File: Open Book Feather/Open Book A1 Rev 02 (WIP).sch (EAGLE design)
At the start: 124 parts, among them J1 SJ-43514-SMT, J2 10118193-0001LF, Q1 DMG341, Q2 IRLML0100, SW1 SPDT_SWITCH, U1 AP2112-3.3, U2 MCP73831T-2ACI/OT, U3 ATSAMD51J64-TQFP(10X10), U4 GD25Q16C (or GD25Q32C), U5 74AC165D, U6 GD25Q16C (or GD25Q32C), U7 23K256-I/SN, U8 MAX4466EXK+T, X1 JSTPH, X2 2x5 0.05" SWD

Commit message: renumber passives, update silkscreen
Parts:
- removed C35: 10uF, microbuilder:CAP_CERAMIC0805-NOOUTLINE
- removed R26, R27: 100K, resistor array:EXB-V8V103JV
- added C13: 1uF, microbuilder:CAP_CERAMIC0805-NOOUTLINE
- added R6: 270, microbuilder:RESISTOR0805_NOOUTLINE
- added R7: 100K, microbuilder:RESISTOR0805_NOOUTLINE
- C17: value 1uF -> 1uF/25V
- C23: value 1uF/25V -> 4.7uF/25V
- C24: value 4.7uF/25V -> 10uF; device microbuilder:CAP_CERAMIC0805-NOOUTLINE -> microbuilder:CAP_CERAMIC0805_10MGAP
- C25: value 10uF -> 1uF
- C26: value 1uF -> 10uF; device microbuilder:CAP_CERAMIC0805_10MGAP -> microbuilder:CAP_CERAMIC0805-NOOUTLINE
- C27: value 10uF -> 1uF; device microbuilder:CAP_CERAMIC0805-NOOUTLINE -> microbuilder:CAP_CERAMIC0805_10MGAP
- C29: value 1uF -> 100uF; device microbuilder:CAP_CERAMIC0805_10MGAP -> resistor:C-USC1210
- C31: value 100uF -> 0.1µF; device resistor:C-USC1210 -> microbuilder:CAP_CERAMIC0805-NOOUTLINE
- C32: value 0.1µF -> 0.01uF
- C33: value 0.01uF -> 100pF
- C34: value 100pF -> 10uF
- R10: value 1M -> 0.47ohm; device microbuilder:RESISTOR0805_NOOUTLINE -> microbuilder:RESISTOR0805_10MGAP
- R11: value 1M -> 100K; device microbuilder:RESISTOR0805_NOOUTLINE -> resistor array:EXB-V8V103JV
- R12: device microbuilder:RESISTOR0805_NOOUTLINE -> resistor array:EXB-V8V103JV
- R13: device microbuilder:RESISTOR0805_NOOUTLINE -> microbuilder:RESISTOR_0805MP
- R14: value 100K -> 1K; device microbuilder:RESISTOR0805_NOOUTLINE -> microbuilder:RESISTOR_0805MP
- R15: value 100K -> 100
- R16: value 0.47ohm -> 100; device microbuilder:RESISTOR0805_10MGAP -> microbuilder:RESISTOR0805_NOOUTLINE
- R17, R18: value 1K -> 100; device microbuilder:RESISTOR_0805MP -> microbuilder:RESISTOR0805_NOOUTLINE
- R19, R20: value 100 -> 1K
- R21, R22: value 100 -> 1M
- R24: value 1K -> 100K
- R8: value 270 -> 100K
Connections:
- net +3V3: now also C13.1, C16.2, C24.1, R11.5, R7.1; no longer C14.1, C17.2, C29.1, R26.5, R9.1
- net A0: now also R15.2; no longer R19.2
- net A1: now also R17.2; no longer R21.2
- net A10_MICAMP: now also C33.1, R24.2; no longer C34.1, R12.2
- net A6_VMEAS: now also R8.2, R9.1; no longer R14.1, R15.2
- net A7_MIC: now also C32.1, R19.1; no longer C33.1, R13.1
- net A8_: now also R13.1; no longer R17.1
- net A9_: now also R14.1; no longer R18.1
- net AGND: now also C31.2, C34.2, R16.1, R18.1, R21.1; no longer C32.2, C35.2, R10.1, R20.1, R22.1
- net AUDIO_LEFT: now also C30.2; no longer C31.2
- net AUDIO_RIGHT: now also C29.2; no longer C30.2
- net AVCC: now also R20.2, R22.2; no longer R11.2, R23.2
- net BUTTON0: now also R12.1; no longer R27.1
- net BUTTON1: now also R12.2; no longer R27.2
- net BUTTON2: now also R12.3; no longer R27.3
- net BUTTON3: now also R12.4; no longer R27.4
- net BUTTON4: now also R11.3; no longer R26.3
- net BUTTON5: now also R11.2; no longer R26.2
- net BUTTON6: now also R11.1; no longer R26.1
- net BUTTON7: now also R11.4; no longer R26.4
- net D13: now also R6.1; no longer R8.1
- net D2_A8: now also R13.2; no longer R17.2
- net D3_A9: now also R14.2; no longer R18.2
- net GND: now also C13.2, C14.1, C21.2, C24.2, R10.2, R11.6, R11.7, R11.8, R12.5, R12.6, R12.7, R12.8, R9.2; no longer C14.2, C21.1, C23.2, C29.2, R14.2, R16.2, R26.6, R26.7, R26.8, R27.5, R27.6, R27.7, R27.8
- net N$15: now also C30.1, R17.1, R18.2; no longer C31.1, R21.1, R22.2
- net N$2: now also C23.2; no longer C24.2
- net N$3: now also C23.1; no longer C24.1
- net N$65: now also C31.1, R19.2, R20.1; no longer C32.1, R13.2, R23.1
- net N$67: now also C32.2, R21.2, R22.1; no longer C33.2, R10.2, R11.1
- net N$68: now also C33.2, R23.1; no longer C34.2, R12.1
- net N$69: now also C34.1, R23.2; no longer C35.1, R24.2
- net N$7: now also R6.2; no longer R8.2
- net N$70: now also C29.1, R15.1, R16.2; no longer C30.1, R19.1, R20.2
- net PREVGH: now also C22.1; no longer C23.1
- net PREVGL: now also C21.1; no longer C22.1
- net QSPI_CS: now also R7.2; no longer R9.2
- net RESE: now also R10.1; no longer R16.1
- net VBAT: now also R8.1; no longer R15.1
- net VCOM: now also C20.2; no longer C21.2
- net VDD: now also C17.2; no longer C18.2
- net VGH: now also C15.2; no longer C16.2
- net VGL: now also C14.2; no longer C15.2
- net VSH: now also C18.2; no longer C19.2
- net VSL: now also C19.2; no longer C20.2
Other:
- note added: "Low pass F3db = 1/R23*C34*2pi"
- note added: "R23"
- note added: "R24"
- note added: "≈ 100x gain"
- note removed: "= ~25-125x gain"
- note removed: "Low pass F3db = 1/R5*C4*2pi"
- note removed: "R5"
- note removed: "VR1+R7"
- moved on the sheet: C14, C15, C16, C17, C18, C19, C20, C21, C22, C23, C24, C25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

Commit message: correct component values
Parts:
- L1: value 68uH -> 10uH
- R4, R6: value 270 -> 1K
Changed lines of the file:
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@@
 <part name="C23" library="microbuilder" deviceset="CAP_CERAMIC" device="0805-NOOUTLINE" value="4.7uF/25V"/>
 <part name="D4" library="microbuilder" deviceset="DIODE-SCHOTTKY" device="SOD-123" value="MBR0530"/>
-<part name="L1" library="microbuilder" deviceset="INDUCTOR" device="NR401" value="68uH"/>
+<part name="L1" library="microbuilder" deviceset="INDUCTOR" device="NR401" value="10uH"/>
 <part name="R10" library="microbuilder" deviceset="RESISTOR" device="0805_10MGAP" value="0.47ohm"/>
 <part name="U$10" library="microbuilder" deviceset="GND" device=""/>
@@
 <part name="R1" library="microbuilder" deviceset="RESISTOR" device="0805_NOOUTLINE" value="10K"/>
 <part name="U2" library="microbuilder" deviceset="MCP73831/2" device="" value="MCP73831T-2ACI/OT"/>
-<part name="R4" library="microbuilder" deviceset="RESISTOR" device="0805_NOOUTLINE" value="270"/>
+<part name="R4" library="microbuilder" deviceset="RESISTOR" device="0805_NOOUTLINE" value="1K"/>
 <part name="C4" library="microbuilder" deviceset="CAP_CERAMIC" device="0805-NOOUTLINE" value="10µF"/>
 <part name="U$33" library="microbuilder" deviceset="GND" device=""/>
@@
 <part name="+3V29" library="supply1" deviceset="+3V3" device=""/>
 <part name="R7" library="microbuilder" deviceset="RESISTOR" device="0805_NOOUTLINE" value="100K"/>
-<part name="R6" library="microbuilder" deviceset="RESISTOR" device="0805_NOOUTLINE" value="270"/>
+<part name="R6" library="microbuilder" deviceset="RESISTOR" device="0805_NOOUTLINE" value="1K"/>
 <part name="GND10" library="supply1" deviceset="GND" device=""/>
 <part name="FB2" library="microbuilder" deviceset="FERRITE" device="0805" value="Ferrite"/>
@@
 <instance part="R6" gate="G$1" x="185.42" y="162.56" smashed="yes" rot="R270">
 <attribute name="NAME" x="187.96" y="162.56" size="1.27" layer="95" font="vector" rot="R270" align="center"/>
-<attribute name="VALUE" x="185.42" y="162.56" size="1.016" layer="96" font="vector" ratio="15" rot="R270" align="center"/>
+<attribute name="VALUE" x="182.88" y="162.56" size="1.016" layer="96" font="vector" ratio="15" rot="R270" align="center"/>
 </instance>
 <instance part="GND10" gate="1" x="185.42" y="142.24" smashed="yes" rot="MR0">

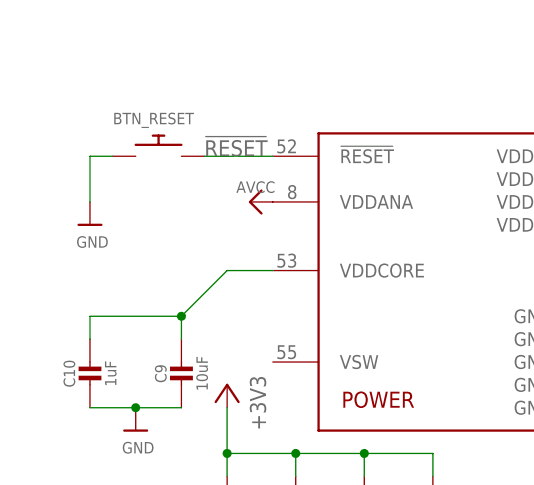
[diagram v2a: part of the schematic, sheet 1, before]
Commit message: restore reset stability circuit
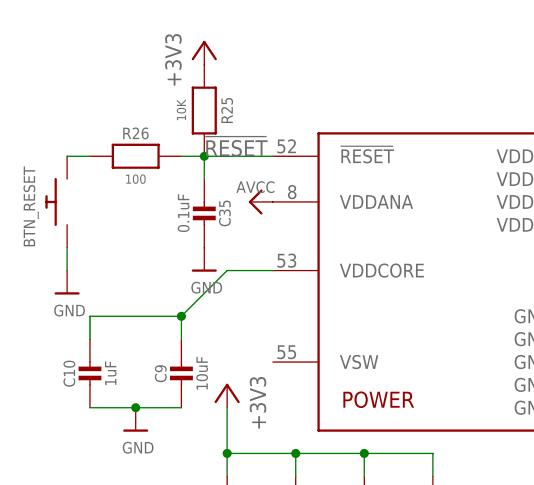
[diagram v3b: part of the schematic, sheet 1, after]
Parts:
- added C35: 0.1uF, microbuilder:CAP_CERAMIC0805_10MGAP
- added R25: 10K, microbuilder:RESISTOR0805_10MGAP
- added R26: 100, microbuilder:RESISTOR0805_10MGAP
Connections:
- new net N$1: BTN_RESET.P$2, R26.1
- net !RESET: now also C35.2, R25.2, R26.2; no longer BTN_RESET.P$2
- net +3V3: now also R25.1
- net GND: now also C35.1
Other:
- moved on the sheet: BTN_RESET
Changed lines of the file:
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@@
 <part name="+3V21" library="supply1" library_urn="urn:adsk.eagle:library:371" deviceset="+3V3" device=""/>
 <part name="GND9" library="supply1" library_urn="urn:adsk.eagle:library:371" deviceset="GND" device=""/>
+<part name="R25" library="microbuilder" deviceset="RESISTOR" device="0805_10MGAP" value="10K"/>
+<part name="C35" library="microbuilder" deviceset="CAP_CERAMIC" device="0805_10MGAP" value="0.1uF"/>
+<part name="+3V6" library="supply1" library_urn="urn:adsk.eagle:library:371" deviceset="+3V3" device=""/>
+<part name="R26" library="microbuilder" deviceset="RESISTOR" device="0805_10MGAP" value="100"/>
+<part name="U$18" library="microbuilder" deviceset="GND" device=""/>
 </parts>
 <sheets>
@@
 <attribute name="VALUE" x="391.16" y="137.16" size="1.016" layer="96" font="vector" ratio="15" rot="R270" align="center"/>
 </instance>
-<instance part="BTN_RESET" gate="G$1" x="325.12" y="165.1" smashed="yes">
-<attribute name="NAME" x="320.04" y="168.656" size="1.27" layer="95"/>
-</instance>
-<instance part="U$24" gate="G$1" x="317.5" y="157.48" smashed="yes">
-<attribute name="VALUE" x="315.976" y="154.94" size="1.27" layer="96"/>
+<instance part="BTN_RESET" gate="G$1" x="314.96" y="160.02" smashed="yes" rot="R90">
+<attribute name="NAME" x="311.404" y="154.94" size="1.27" layer="95" rot="R90"/>
+</instance>
+<instance part="U$24" gate="G$1" x="314.96" y="149.86" smashed="yes">
+<attribute name="VALUE" x="313.436" y="147.32" size="1.27" layer="96"/>
 </instance>
 <instance part="U$6" gate="G$1" x="444.5" y="172.72" smashed="yes">
@@
 </instance>
 <instance part="MS1" gate="G$1" x="492.76" y="81.28" smashed="yes" rot="R270"/>
+<instance part="R25" gate="G$1" x="330.2" y="170.18" smashed="yes" rot="R270">
+<attribute name="NAME" x="332.74" y="170.18" size="1.27" layer="95" font="vector" rot="R270" align="center"/>
+<attribute name="VALUE" x="327.66" y="170.18" size="1.016" layer="96" font="vector" ratio="15" rot="R270" align="center"/>
+</instance>
+<instance part="C35" gate="G$1" x="330.2" y="160.02" smashed="yes" rot="R180">
+<attribute name="NAME" x="332.49" y="158.77" size="1.27" layer="95" font="vector" rot="R270" align="center"/>
+<attribute name="VALUE" x="327.9" y="158.77" size="1.27" layer="96" font="vector" rot="R270" align="center"/>
+</instance>
+<instance part="+3V6" gate="G$1" x="330.2" y="177.8" smashed="yes">
+<attribute name="VALUE" x="327.66" y="172.72" size="1.778" layer="96" rot="R90"/>
+</instance>
+<instance part="R26" gate="G$1" x="322.58" y="165.1" smashed="yes">
+<attribute name="NAME" x="322.58" y="167.64" size="1.27" layer="95" font="vector" align="center"/>
+<attribute name="VALUE" x="322.58" y="162.56" size="1.016" layer="96" font="vector" ratio="15" align="center"/>
+</instance>
+<instance part="U$18" gate="G$1" x="330.2" y="152.4" smashed="yes">
+<attribute name="VALUE" x="328.676" y="149.86" size="1.27" layer="96"/>
+</instance>
 </instances>
 <busses>
@@
 <segment>
 <pinref part="U$24" gate="G$1" pin="GND"/>
+<wire x1="314.96" y1="154.94" x2="314.96" y2="152.4" width="0.1524" layer="91"/>
 <pinref part="BTN_RESET" gate="G$1" pin="P$1"/>
-<wire x1="320.04" y1="165.1" x2="317.5" y2="165.1" width="0.1524" layer="91"/>
-<wire x1="317.5" y1="165.1" x2="317.5" y2="160.02" width="0.1524" layer="91"/>
 </segment>
 <segment>
@@
 <wire x1="487.68" y1="38.1" x2="472.44" y2="38.1" width="0.1524" layer="91"/>
 <wire x1="472.44" y1="38.1" x2="472.44" y2="35.56" width="0.1524" layer="91"/>
+</segment>
+<segment>
+<pinref part="C35" gate="G$1" pin="1"/>
+<pinref part="U$18" gate="G$1" pin="GND"/>
 </segment>
 </net>
@@
 <wire x1="467.36" y1="73.66" x2="487.68" y2="73.66" width="0.1524" layer="91"/>
 </segment>
+<segment>
+<pinref part="R25" gate="G$1" pin="1"/>
+<pinref part="+3V6" gate="G$1" pin="+3V3"/>
+</segment>
 </net>
 <net name="AVCC" class="1">
@@
 </segment>
 <segment>
+<pinref part="C35" gate="G$1" pin="2"/>
+<pinref part="R25" gate="G$1" pin="2"/>
+<wire x1="330.2" y1="162.56" x2="330.2" y2="165.1" width="0.1524" layer="91"/>
+<junction x="330.2" y="165.1"/>
+<wire x1="330.2" y1="165.1" x2="337.82" y2="165.1" width="0.1524" layer="91"/>
+<pinref part="R26" gate="G$1" pin="2"/>
+<wire x1="330.2" y1="165.1" x2="327.66" y2="165.1" width="0.1524" layer="91"/>
+<label x="330.2" y="165.1" size="1.778" layer="95"/>
 <pinref part="U3" gate="G$3" pin="!RESET"/>
-<label x="330.2" y="165.1" size="1.778" layer="95"/>
-<pinref part="BTN_RESET" gate="G$1" pin="P$2"/>
-<wire x1="330.2" y1="165.1" x2="337.82" y2="165.1" width="0.1524" layer="91"/>
 </segment>
 </net>
@@
 </segment>
 </net>
+<net name="N$1" class="0">
+<segment>
+<pinref part="BTN_RESET" gate="G$1" pin="P$2"/>
+<pinref part="R26" gate="G$1" pin="1"/>
+<wire x1="314.96" y1="165.1" x2="317.5" y2="165.1" width="0.1524" layer="91"/>
+</segment>
+</net>
